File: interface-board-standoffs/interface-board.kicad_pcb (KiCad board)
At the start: 2 copper layers, 181.5 x 110 mm, 83 parts, among them J1 HECS, J11 UART, J12 NTC1, J13 NTC1, J15 ICSP, J16 AMPSEAL, J2 CASEFAN1, J3 CASEFAN2, J4 Bender-LV, J5 BLINKY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

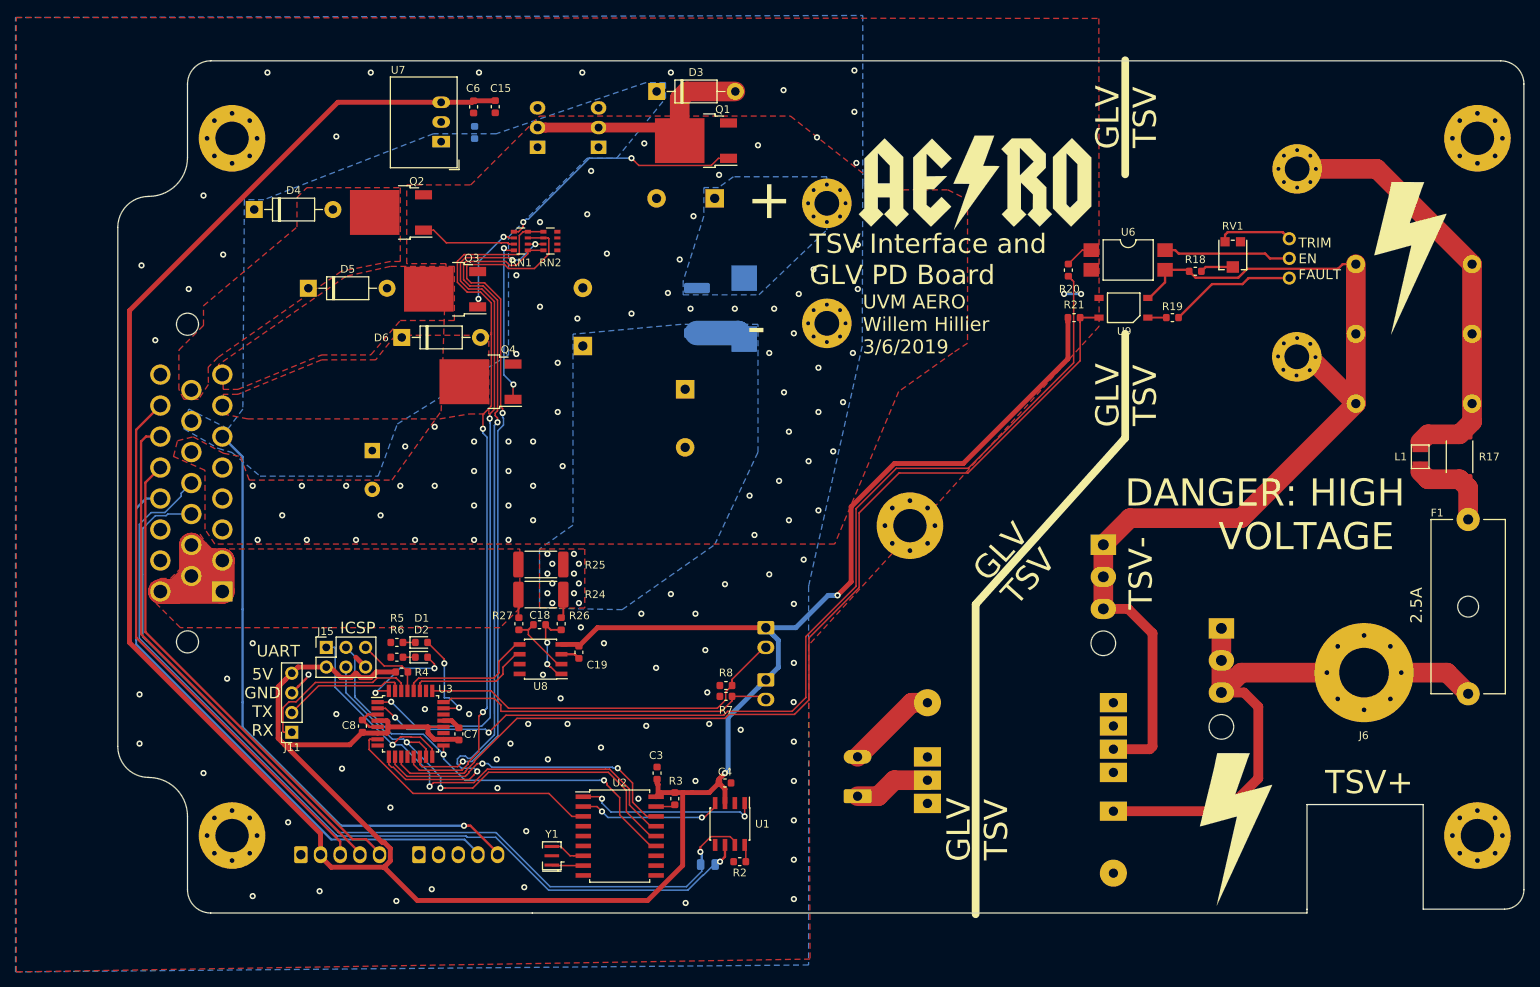
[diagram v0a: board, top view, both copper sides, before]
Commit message: Made rev1.1 of interface-board
Added i2c pullups, fixed chip pinout, added isolation slot, removed secondary DC/DC converter
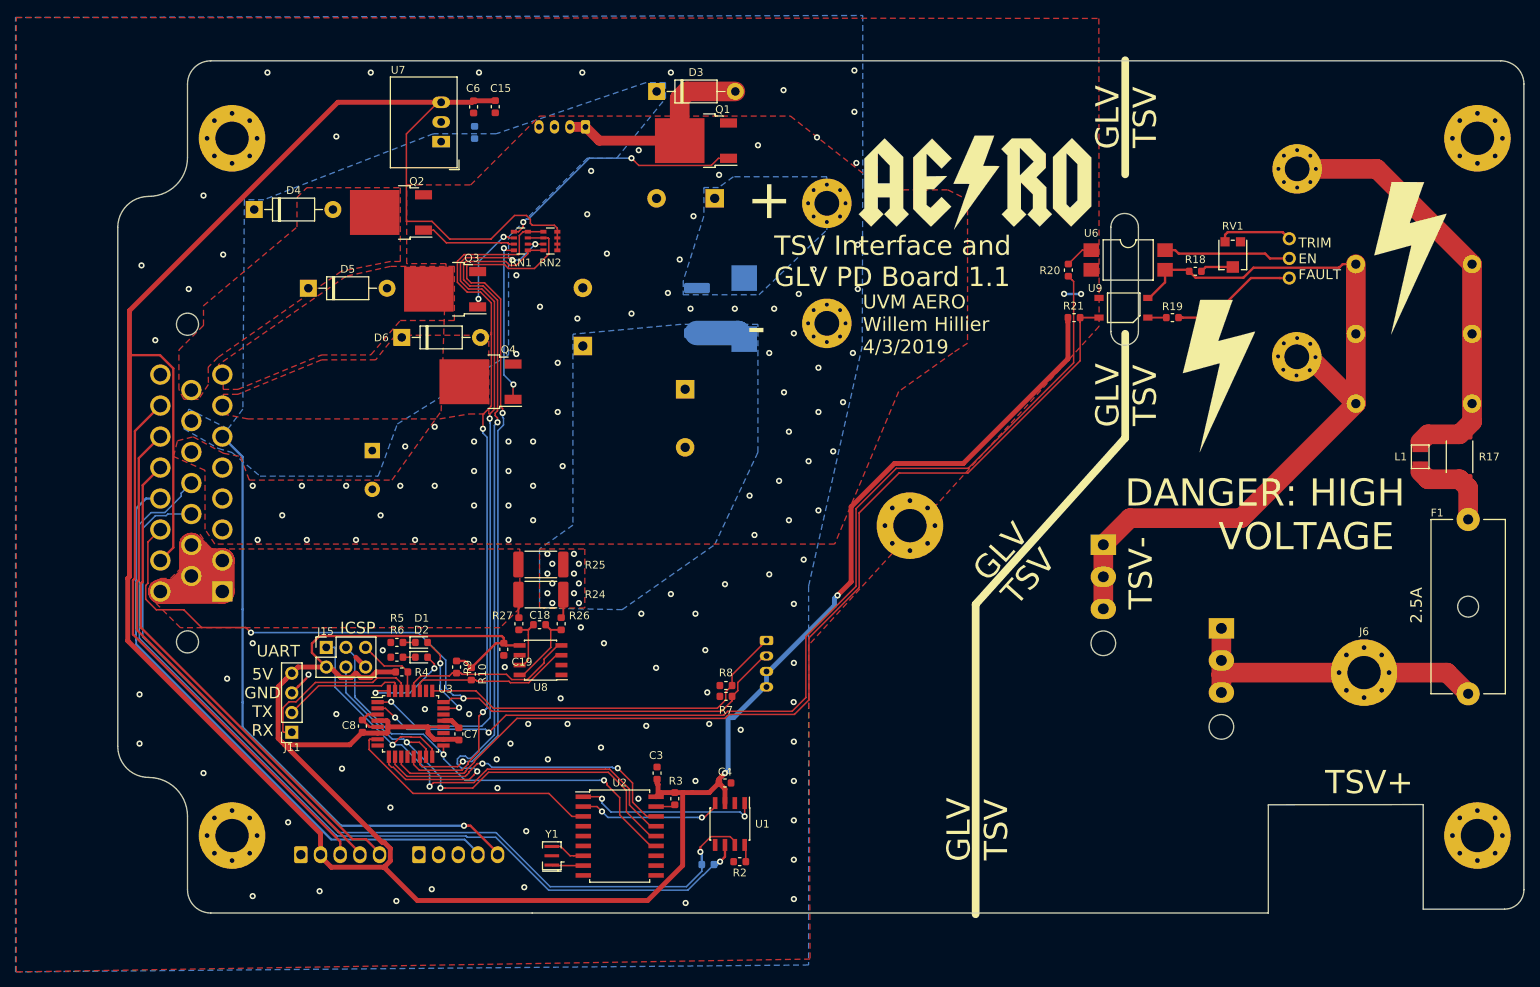
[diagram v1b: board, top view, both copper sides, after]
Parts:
- removed J12, J13: NTC1, Connector_Molex:Molex_KK-254_AE-6410-02A_1x02_P2.54mm_Vertical
- removed J5: BLINKY, Connector_Phoenix_MC_HighVoltage:PhoenixContact_MCV_1,5_2-G-5.08_1x02_P5.08mm_Vertical
- removed U10: EPM1510SJ, CustomFootprints:EPM1510SJ
- added R10: 10k, Resistor_SMD:R_0603_1608Metric, F.Cu at (98.1, 118.3)
- added R9: 10k, Resistor_SMD:R_0603_1608Metric, F.Cu at (96.2, 117.4)
- J16: value AMPSEAL -> Conn_01x23
- J2: value CASEFAN1 -> FANS; footprint Connector:FanPinHeader_1x03_P2.54mm_Vertical -> Connector_JST:JST_PH_B4B-PH-K_1x04_P2.00mm_Vertical
- J3: value CASEFAN2 -> NTCs; footprint Connector:FanPinHeader_1x03_P2.54mm_Vertical -> Connector_JST:JST_PH_B4B-PH-K_1x04_P2.00mm_Vertical
- J6: footprint MountingHole:MountingHole_6.4mm_M6_Pad_Via -> MountingHole:MountingHole_4.3mm_M4_Pad_Via
- R1: footprint Resistor_SMD:R_0805_2012Metric -> Resistor_SMD:R_0603_1608Metric
- moved G*** 86.2 mm to (165.4, 64.7), turned to 90 degrees
- moved G*** 71.3 mm to (193.3, 67.2)
- moved J3 67.3 mm to (136.2, 113.9), turned to 270 degrees
- moved G*** 58.5 mm to (194.6, 79.9)
- moved C19 9.70 mm to (102.3, 115.1)
- moved J2 6.72 mm to (112.8, 47.7), turned to 180 degrees
- moved U8 0.13 mm to (107.0, 116.5)
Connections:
- net /Main/IMD_AN1 renamed /Main/HECS_AN1
- net /Main/IMD_AN2 renamed /Main/HECS_AN2
- net /Main/IMD_AN3 renamed /Main/HECS_AN3
- J16 pad 17: (no net) -> +5V
- J16 pad 18: (no net) -> /Main/TEMP_1
- J2 pad 1: +12V -> /Main/FANOUT0
- J2 pad 3: (no net) -> +12V
- J3 pad 1: +12V -> /Main/TEMP_2
- J3 pad 2: /Main/FANOUT0 -> /Main/TEMP_1
- J3 pad 3: (no net) -> +5V
- RN2 pad 1: GND -> +5V
- RN2 pad 2: GND -> +5V
- RN2 pad 3: GND -> +5V
- RN2 pad 4: GND -> +5V
- U8 pad 1: Net-(C18-Pad1) -> GND
- U8 pad 2: Net-(C18-Pad2) -> GND
- U8 pad 3: GND -> SDA
- U8 pad 4: +5V -> SCL
- U8 pad 5: SCL -> +5V
- U8 pad 6: SDA -> GND
- U8 pad 7: GND -> Net-(C18-Pad2)
- U8 pad 8: GND -> Net-(C18-Pad1)
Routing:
- net +5V: track 406.8 -> 490.4 mm
- net /Main/TEMP_1: track 44.3 -> 104.7 mm, vias 0 -> 2
- net /Main/HV+: track 79.3 -> 41.4 mm
- net /Main/HV-: track 134.7 -> 107.2 mm
- net Net-(J5-Pad2): track 11.9 -> 0.00 mm
- net Net-(J5-Pad1): track 9.88 -> 0.00 mm
- net SCL: track 17.6 -> 23.3 mm
- net SDA: track 16.0 -> 21.2 mm
- net GND: track 16.1 -> 13.6 mm
- net /Main/FANOUT0: track 32.0 -> 30.3 mm
- net Net-(C18-Pad2): track 8.62 -> 7.44 mm
- net /Main/TEMP_2: track 48.3 -> 49.1 mm
- net /Main/HECS_AN2: track 67.8 -> 67.2 mm
- net /Main/sheet5C830478/FAULT_HV: track 16.4 -> 17.0 mm
- net Net-(C18-Pad1): track 10.4 -> 10.6 mm, vias 2 -> 0
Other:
- outline, holes or cut-outs redrawn
- board text added: "- - + +"
- board text added: "2 1 5V 5V Thermistor"
- board text added: "TSV Interface and GLV PD Board 1.1"
- board text added: "UVM AERO Willem Hillier 4/3/2019"
- board text removed: "2 1 Thermistor"
- board text removed: "TSV Indicator"
- board text removed: "TSV Interface and GLV PD Board"
- board text removed: "UVM AERO Willem Hillier 3/6/2019"
